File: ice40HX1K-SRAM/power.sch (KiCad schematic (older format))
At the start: 13 parts

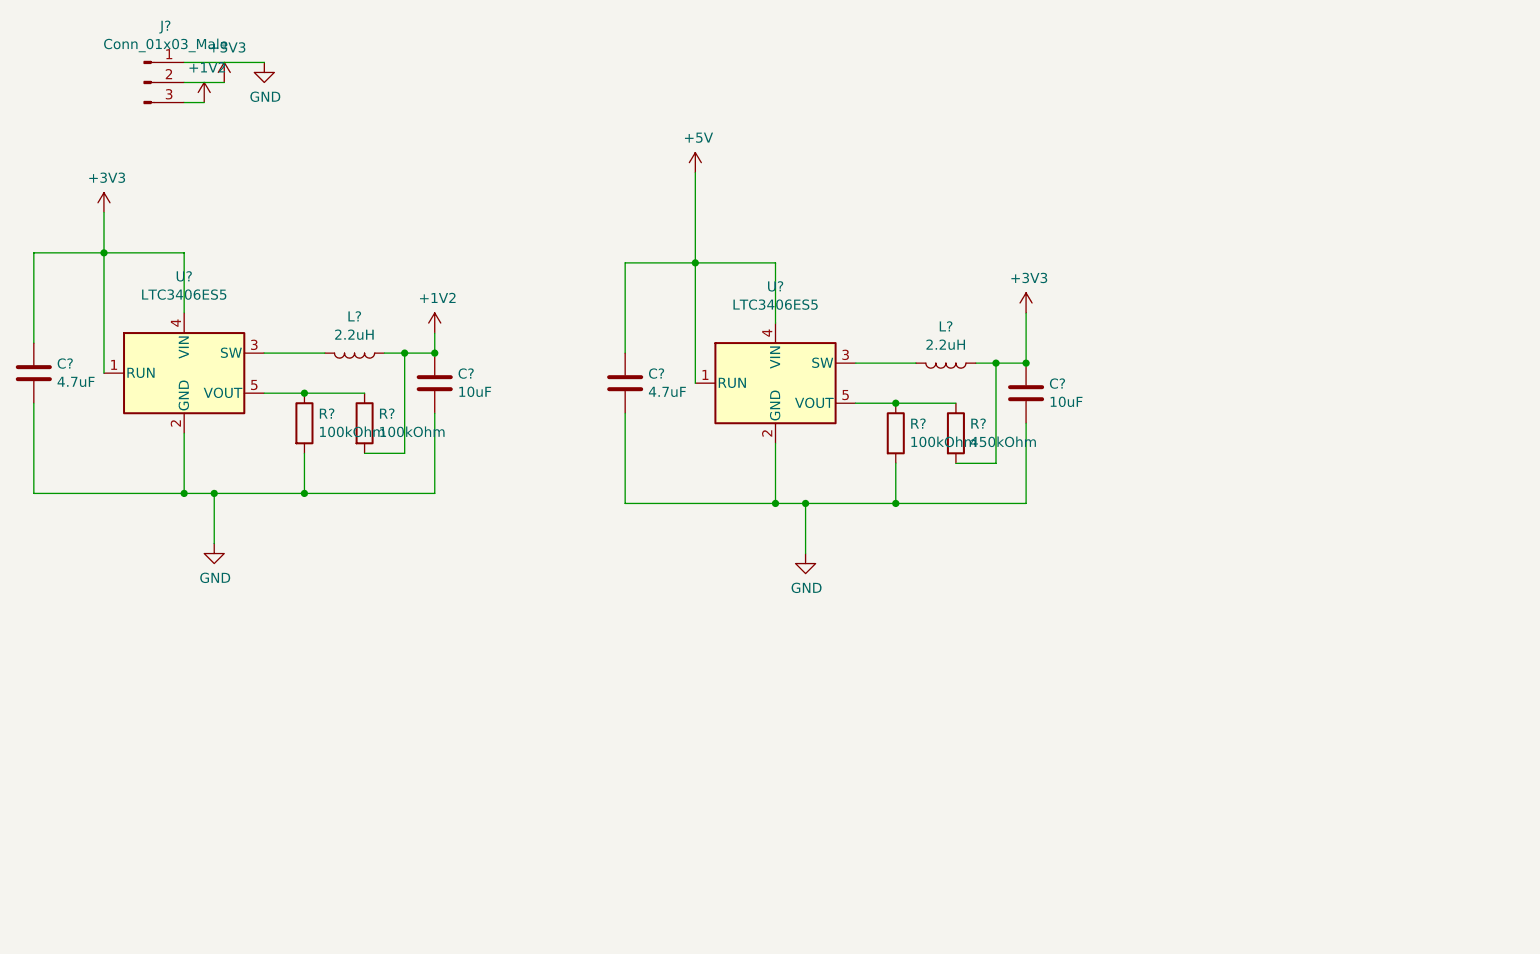
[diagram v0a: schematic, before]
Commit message: add MAX40203 in power supply of the ice40 ice40HX1K fpga to OR supply USB/battery cell
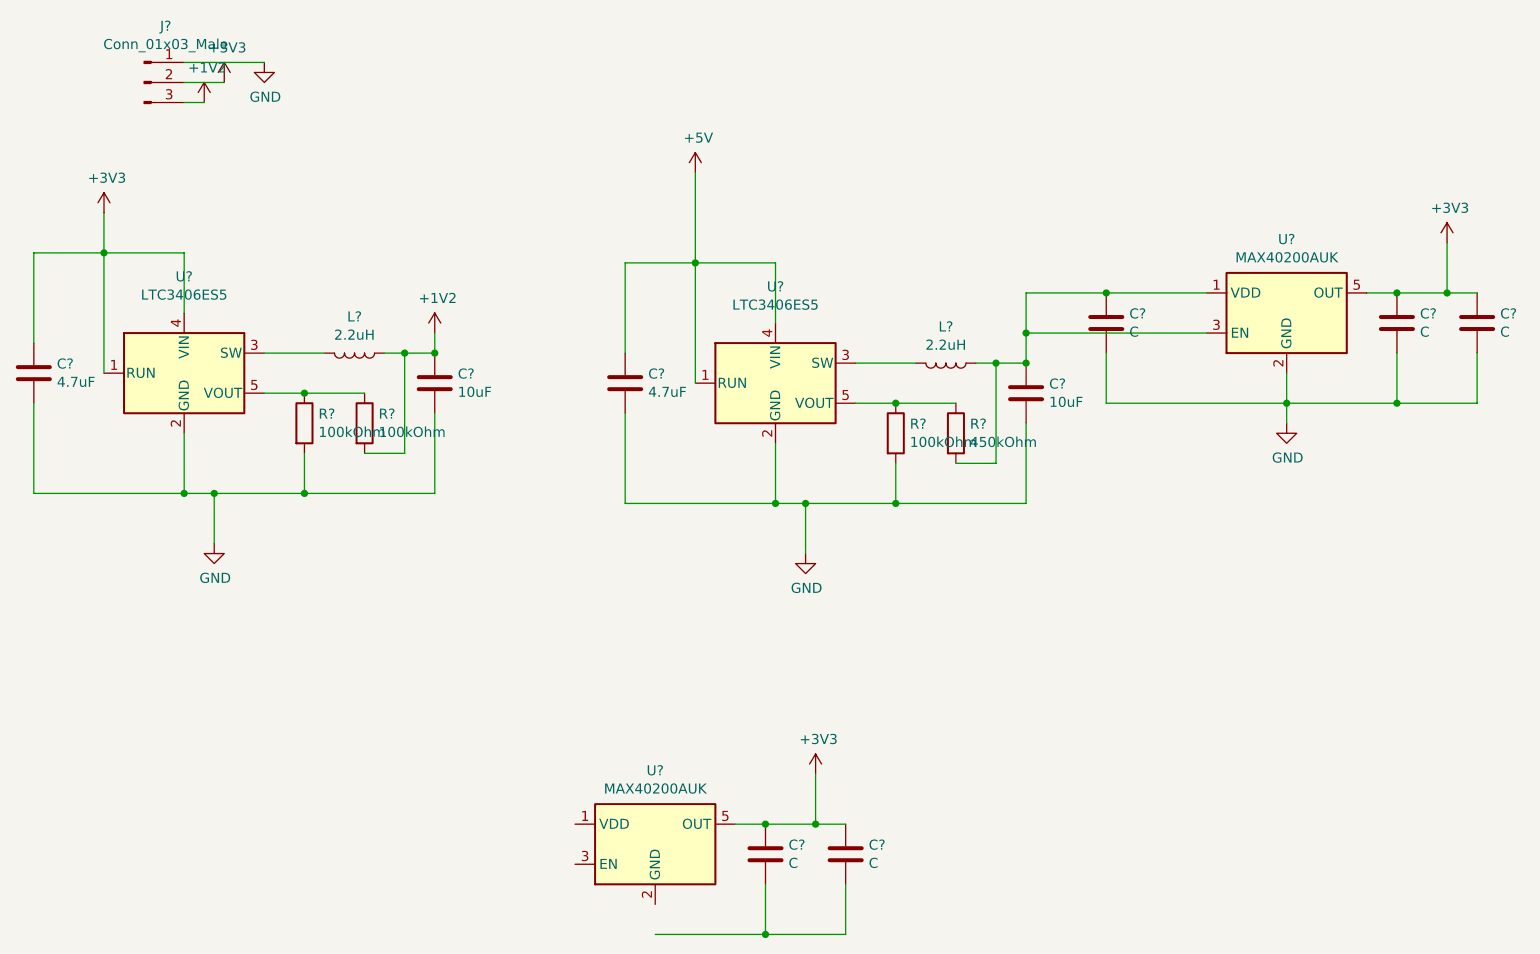
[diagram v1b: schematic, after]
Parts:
- added C? (x5): C, symbol Device:C
- added U? (x2): MAX40200AUK, Package_TO_SOT_SMD:SOT-23-5, symbol Analog_Switch:MAX40200AUK
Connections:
- net +3V3: now also C?.1, C?.1, C?.1, C?.1, U?.5 (OUT), U?.5 (OUT); no longer C?.1, L?.1, R?.2
- net GND: now also C?.2, C?.2, C?.2, U?.2 (GND)
- new net: C?.1, C?.1, L?.1, R?.2, U?.1 (VDD), U?.3 (EN)
- new net: C?.2, C?.2
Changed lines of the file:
@@
 	6050 3150 6050 2750
 Connection ~ 5400 3150
-Connection ~ 6050 2450
 $Comp
 L power:GND #PWR?
@@
 	4950 3150 5400 3150
 $Comp
-L power:+3V3 #PWR?
-U 1 1 5E5F5466
-P 6050 2200
-F 0 "#PWR?" H 6050 2050 50  0001 C CNN
-F 1 "+3V3" H 6065 2373 50  0000 C CNN
-F 2 "" H 6050 2200 50  0001 C CNN
-F 3 "" H 6050 2200 50  0001 C CNN
-	1    6050 2200
-	1    0    0    -1
-$EndComp
-Wire Wire Line
-	6050 2200 6050 2450
-$Comp
 L power:+5V #PWR?
 U 1 1 5E5F763C
@@
 Wire Wire Line
 	4400 1500 4400 1950
+$Comp
+L Analog_Switch:MAX40200AUK U?
+U 1 1 5E608631
+P 4200 4850
+F 0 "U?" H 4200 5217 50  0000 C CNN
+F 1 "MAX40200AUK" H 4200 5126 50  0000 C CNN
+F 2 "Package_TO_SOT_SMD:SOT-23-5" H 4200 5350 50  0001 C CNN
+F 3 "https://datasheets.maximintegrated.com/en/ds/MAX40200.pdf" H 4200 5350 50  0001 C CNN
+	1    4200 4850
+	1    0    0    -1
+$EndComp
+$Comp
+L Analog_Switch:MAX40200AUK U?
+U 1 1 5E608F29
+P 7350 2200
+F 0 "U?" H 7350 2567 50  0000 C CNN
+F 1 "MAX40200AUK" H 7350 2476 50  0000 C CNN
+F 2 "Package_TO_SOT_SMD:SOT-23-5" H 7350 2700 50  0001 C CNN
+F 3 "https://datasheets.maximintegrated.com/en/ds/MAX40200.pdf" H 7350 2700 50  0001 C CNN
+	1    7350 2200
+	1    0    0    -1
+$EndComp
+$Comp
+L power:+3V3 #PWR?
+U 1 1 5E60C10F
+P 8150 1850
+F 0 "#PWR?" H 8150 1700 50  0001 C CNN
+F 1 "+3V3" H 8165 2023 50  0000 C CNN
+F 2 "" H 8150 1850 50  0001 C CNN
+F 3 "" H 8150 1850 50  0001 C CNN
+	1    8150 1850
+	1    0    0    -1
+$EndComp
+Wire Wire Line
+	8150 1850 8150 2100
+Wire Wire Line
+	6050 2450 6050 2300
+Wire Wire Line
+	6050 2100 6450 2100
+Connection ~ 6050 2450
+Wire Wire Line
+	6050 2300 6950 2300
+Connection ~ 6050 2300
+Wire Wire Line
+	6050 2300 6050 2100
+$Comp
+L Device:C C?
+U 1 1 5E60FC3E
+P 6450 2250
+F 0 "C?" H 6565 2296 50  0000 L CNN
+F 1 "C" H 6565 2205 50  0000 L CNN
+F 2 "" H 6488 2100 50  0001 C CNN
+F 3 "~" H 6450 2250 50  0001 C CNN
+	1    6450 2250
+	1    0    0    -1
+$EndComp
+Connection ~ 6450 2100
+Wire Wire Line
+	6450 2100 6950 2100
+$Comp
+L Device:C C?
+U 1 1 5E61086D
+P 7900 2250
+F 0 "C?" H 8015 2296 50  0000 L CNN
+F 1 "C" H 8015 2205 50  0000 L CNN
+F 2 "" H 7938 2100 50  0001 C CNN
+F 3 "~" H 7900 2250 50  0001 C CNN
+	1    7900 2250
+	1    0    0    -1
+$EndComp
+$Comp
+L Device:C C?
+U 1 1 5E610C79
+P 8300 2250
+F 0 "C?" H 8415 2296 50  0000 L CNN
+F 1 "C" H 8415 2205 50  0000 L CNN
+F 2 "" H 8338 2100 50  0001 C CNN
+F 3 "~" H 8300 2250 50  0001 C CNN
+	1    8300 2250
+	1    0    0    -1
+$EndComp
+Wire Wire Line
+	7750 2100 7900 2100
+Connection ~ 7900 2100
+Wire Wire Line
+	7900 2100 8150 2100
+Connection ~ 8150 2100
+Wire Wire Line
+	8150 2100 8300 2100
+$Comp
+L power:GND #PWR?
+U 1 1 5E6126DE
+P 7350 2750
+F 0 "#PWR?" H 7350 2500 50  0001 C CNN
+F 1 "GND" H 7355 2577 50  0000 C CNN
+F 2 "" H 7350 2750 50  0001 C CNN
+F 3 "" H 7350 2750 50  0001 C CNN
+	1    7350 2750
+	1    0    0    -1
+$EndComp
+Wire Wire Line
+	7350 2500 7350 2650
+Wire Wire Line
+	6450 2400 6450 2650
+Wire Wire Line
+	6450 2650 7350 2650
+Connection ~ 7350 2650
+Wire Wire Line
+	7350 2650 7350 2750
+Wire Wire Line
+	8300 2400 8300 2650
+Wire Wire Line
+	8300 2650 7900 2650
+Wire Wire Line
+	7900 2400 7900 2650
+Connection ~ 7900 2650
+Wire Wire Line
+	7900 2650 7350 2650
+$Comp
+L power:+3V3 #PWR?
+U 1 1 5E61F7B9
+P 5000 4500
+F 0 "#PWR?" H 5000 4350 50  0001 C CNN
+F 1 "+3V3" H 5015 4673 50  0000 C CNN
+F 2 "" H 5000 4500 50  0001 C CNN
+F 3 "" H 5000 4500 50  0001 C CNN
+	1    5000 4500
+	1    0    0    -1
+$EndComp
+Wire Wire Line
+	5000 4500 5000 4750
+$Comp
+L Device:C C?
+U 1 1 5E61F7C0
+P 4750 4900
+F 0 "C?" H 4865 4946 50  0000 L CNN
+F 1 "C" H 4865 4855 50  0000 L CNN
+F 2 "" H 4788 4750 50  0001 C CNN
+F 3 "~" H 4750 4900 50  0001 C CNN
+	1    4750 4900
+	1    0    0    -1
+$EndComp
+$Comp
+L Device:C C?
+U 1 1 5E61F7C6
+P 5150 4900
+F 0 "C?" H 5265 4946 50  0000 L CNN
+F 1 "C" H 5265 4855 50  0000 L CNN
+F 2 "" H 5188 4750 50  0001 C CNN
+F 3 "~" H 5150 4900 50  0001 C CNN
+	1    5150 4900
+	1    0    0    -1
+$EndComp
+Wire Wire Line
+	4600 4750 4750 4750
+Connection ~ 4750 4750
+Wire Wire Line
+	4750 4750 5000 4750
+Connection ~ 5000 4750
+Wire Wire Line
+	5000 4750 5150 4750
+Wire Wire Line
+	5150 5050 5150 5300
+Wire Wire Line
+	5150 5300 4750 5300
+Wire Wire Line
+	4750 5050 4750 5300
+Connection ~ 4750 5300
+Wire Wire Line
+	4750 5300 4200 5300
 $EndSCHEMATC
